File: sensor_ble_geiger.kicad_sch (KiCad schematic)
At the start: 23 parts

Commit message: power source
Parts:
- added C?: 10uF, symbol Device:C
- added C?: 33nF, symbol Device:C
- added C?: C_Polarized, symbol Device:C_Polarized
- added D?: MBRS120, symbol Device:D_Schottky
- added L?: 4.7uH, symbol Device:L
- added R?: 100k, symbol Device:R
- added R?: 47k, symbol Device:R
- added R?: 309K, symbol Device:R
- added U?: LT1308, symbol _linear-regulators:LT1308
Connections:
- net GNDD: now also C?.2, C?.2, C?.2, R?.2, U?.4 (GND)
- net VCC_5V: now also C?.1, D?.1 (K), R?.2
- new net: R?.1, R?.1, U?.2 (FB)
- new net: D?.2 (A), L?.2, U?.5 (SW)
- new net: R?.1, U?.1 (VC)
- new net: C?.1, R?.2
- new net 18660_Input: C?.1, L?.1, U?.3 (~SHDN), U?.6 (VIN)

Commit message: Добавлена разводка
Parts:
- added BZ1: Buzzer, Buzzer_Beeper:Buzzer_15x7.5RM7.6, symbol Device:Buzzer
- added C6: 470pF, Capacitor_SMD:C_0805_2012Metric, symbol Device:C
- added C8: 2.2uF, Capacitor_SMD:C_0805_2012Metric, symbol Device:C
- added D5: LED, LED_THT:LED_D3.0mm, symbol Device:LED
- added J1: Conn_01x02, Connector_PinHeader_2.54mm:PinHeader_1x02_P2.54mm_Vertical, symbol Connector_Generic:Conn_01x02
- added J2: Geiger +, Geiger:Датчик, symbol Connector_Generic:Conn_01x01
- added J3: Geiger -, Geiger:Датчик, symbol Connector_Generic:Conn_01x01
- added J4: Conn_01x04, Connector_PinHeader_2.54mm:PinHeader_1x04_P2.54mm_Horizontal, symbol Connector_Generic:Conn_01x04
- added Q4: BC847, Package_TO_SOT_SMD:SOT-23, symbol Transistor_BJT:BC847
- added R13: 510R, Resistor_SMD:R_0805_2012Metric, symbol Device:R
- added R15: 1K, Resistor_SMD:R_0805_2012Metric, symbol Device:R
- added U3: MIC5219-3.3, Package_TO_SOT_SMD:SOT-23-5, symbol Paperless_v3-rescue:MIC5219-3.3-Regulator_Linear
- added U4: E73-2G4M04S1B, Ebyte:E73-2G4M04S1B, symbol Ebyte:E73-2G4M04S1B
- C1, C11, C3, C4: renamed from C?; footprint (none) -> Resistor_SMD:R_0805_2012Metric
- C10, C7, C9: renamed from C?; footprint (none) -> Resistor_SMD:R_1210_3225Metric
- C2: renamed from C?; footprint (none) -> Resistor_THT:R_Axial_DIN0204_L3.6mm_D1.6mm_P5.08mm_Horizontal
- C5: renamed from C?; value C_Polarized -> 100uF; footprint (none) -> Resistor_THT:R_Axial_DIN0204_L3.6mm_D1.6mm_P5.08mm_Horizontal
- D1: renamed from D?; footprint (none) -> Diode_SMD:D_SMB
- L1: renamed from L?; footprint (none) -> Geiger:IND_SMD_CD43
- L2: renamed from L?; footprint (none) -> Geiger:BOURNS-SDR0503
- R1, R10, R11, R12, R2, R3, R4, R5, R6, R7, R8, R9: renamed from R?; footprint (none) -> Resistor_SMD:R_0805_2012Metric
- U2: renamed from U?; footprint (none) -> Package_SO:SO-8_5.3x6.2mm_P1.27mm
- gave numbers to parts that had none: 7
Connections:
- net 18660_Input: now also J1.2 (Pin_2), U3.1 (IN), U3.3 (EN)
- net GNDD: now also C6.2, C8.2, D5.1 (K), J1.1 (Pin_1), J4.4 (Pin_4), Q4.2 (E), U3.2 (GND), U4.1 (GND), U4.16 (GND), U4.2 (GND), U4.3 (GND), U4.43 (GND), U4.44 (GND)
- net INT_0: now reaches Q3.3 (C), R8.1
- net INT_0: now also U4.22 (P0.06)
- net at R10.2: now also J2.1 (Pin_1)
- net at C11.1, R11.1: now also J3.1 (Pin_1)
- net VCC_3.3 renamed VCC_3.3V
- net VCC_3.3V: now also BZ1.1 (-), C8.1, J4.1 (Pin_1), U3.5 (OUT), U4.17 (VCC)
- new net: J4.2 (Pin_2), U4.39 (SWDIO)
- new net: J4.3 (Pin_3), U4.38 (SWDCLK)
- new net: C6.1, U3.4 (BP)
- new net: Q4.1 (B), R15.1
- new net: BZ1.2 (+), Q4.3 (C)
- new net: D5.2 (A), R13.1
- new net BUZZER: R15.2, U4.23 (P0.07)
- new net LED: R13.2, U4.24 (P0.08)
- no-connect marks 0 -> 34

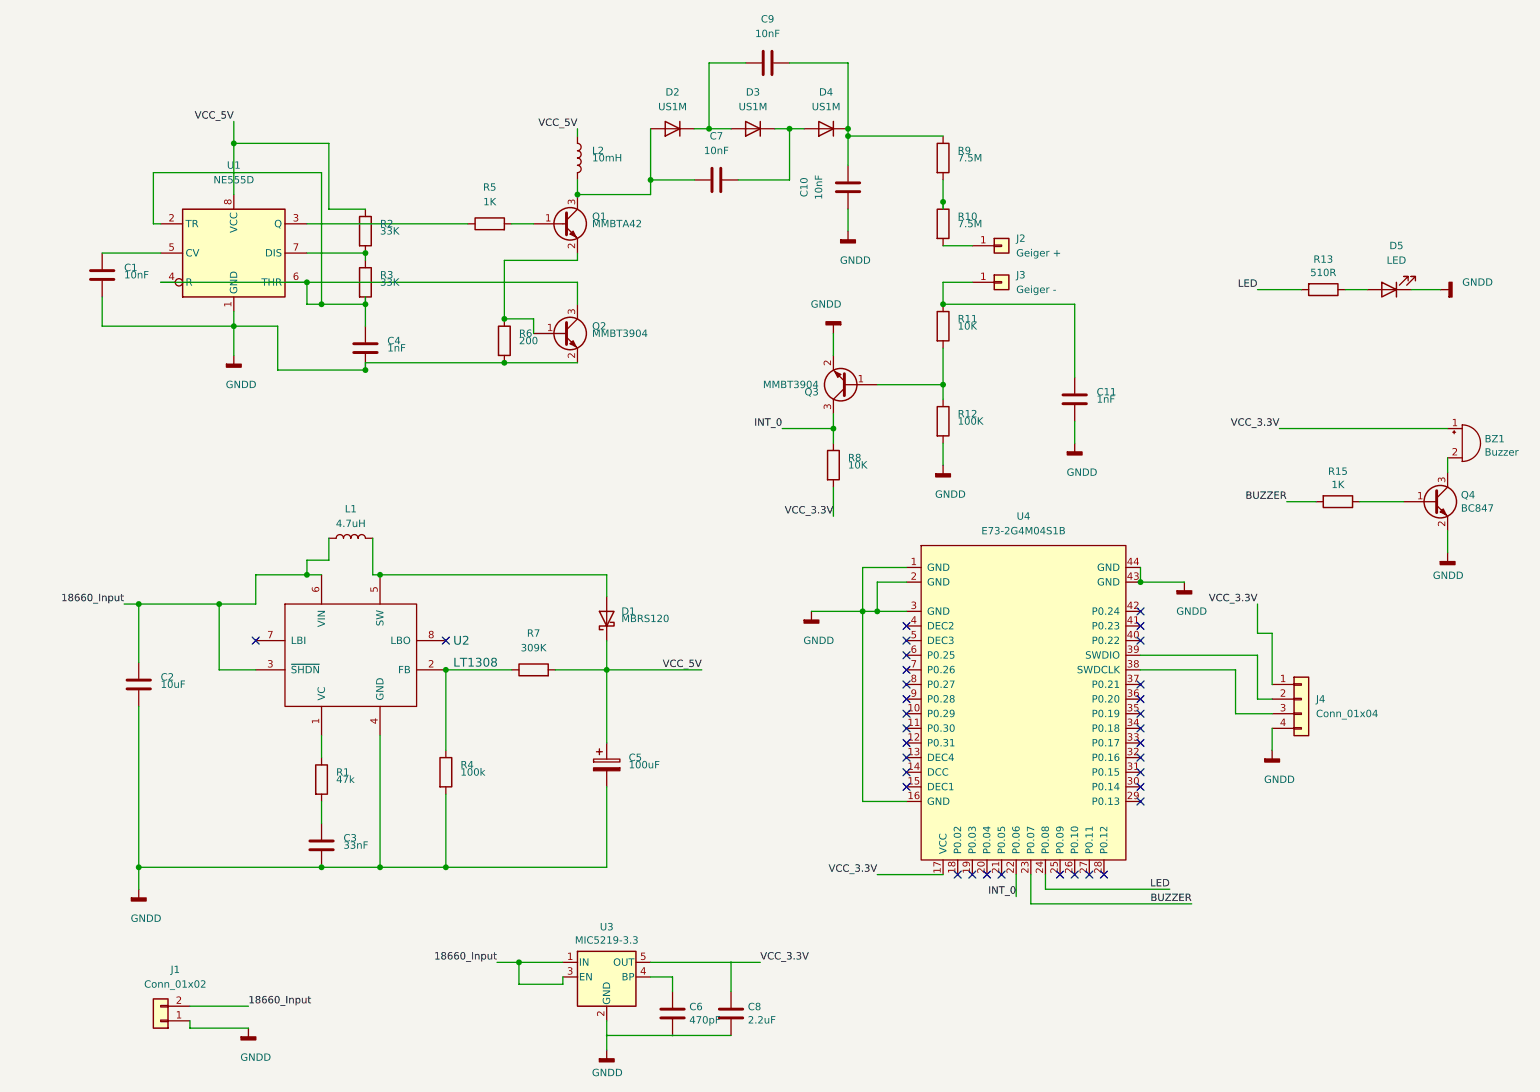
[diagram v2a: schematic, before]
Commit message: Move to 3.3V
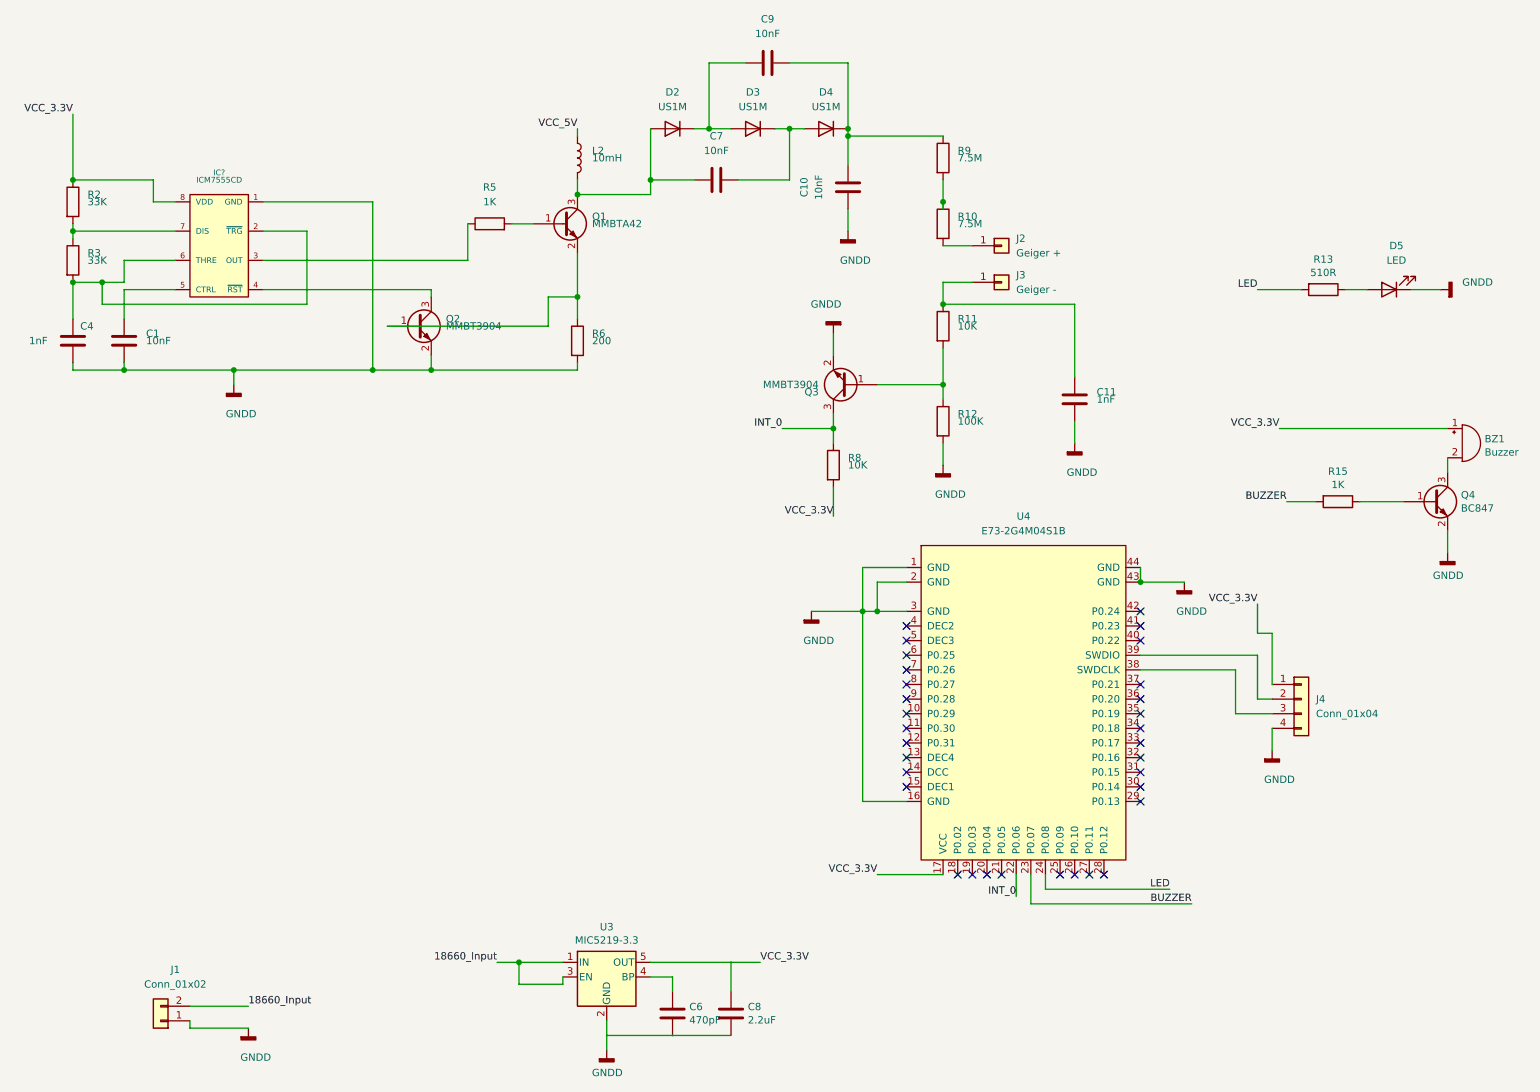
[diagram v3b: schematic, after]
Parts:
- removed C2: 10uF, Resistor_THT:R_Axial_DIN0204_L3.6mm_D1.6mm_P5.08mm_Horizontal, symbol Device:C
- removed C3: 33nF, Resistor_SMD:R_0805_2012Metric, symbol Device:C
- removed C5: 100uF, Resistor_THT:R_Axial_DIN0204_L3.6mm_D1.6mm_P5.08mm_Horizontal, symbol Device:C_Polarized
- removed D1: MBRS120, Diode_SMD:D_SMB, symbol Device:D_Schottky
- removed L1: 4.7uH, Geiger:IND_SMD_CD43, symbol Device:L
- removed R1: 47k, Resistor_SMD:R_0805_2012Metric, symbol Device:R
- removed R4: 100k, Resistor_SMD:R_0805_2012Metric, symbol Device:R
- removed R7: 309K, Resistor_SMD:R_0805_2012Metric, symbol Device:R
- removed U1: NE555D, Package_SO:SOIC-8_3.9x4.9mm_P1.27mm, symbol Timer:NE555D
- removed U2: LT1308, Package_SO:SO-8_5.3x6.2mm_P1.27mm, symbol _linear-regulators:LT1308
- added IC?: ICM7555CD, symbol ICM:ICM7555CD
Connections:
- net GNDD: now also IC?.1 (GND)
- net VCC_3.3V: now also R2.1, IC?.8 (VDD)
- net VCC_5V: no longer R2.1
- net at R2.2, R3.1: now also IC?.7 (DIS)
- net at C4.1, R3.2: now also IC?.2 (~TRG), IC?.6 (THRE); no longer Q2.3 (C)
- net at R5.1: now also IC?.3 (OUT)
- net at C1.1: now also IC?.5 (CTRL)
- new net: IC?.4 (~RST), Q2.3 (C)
- no-connect marks 34 -> 32
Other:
- moved on the sheet: C1, C4, Q2, R2, R3, R6

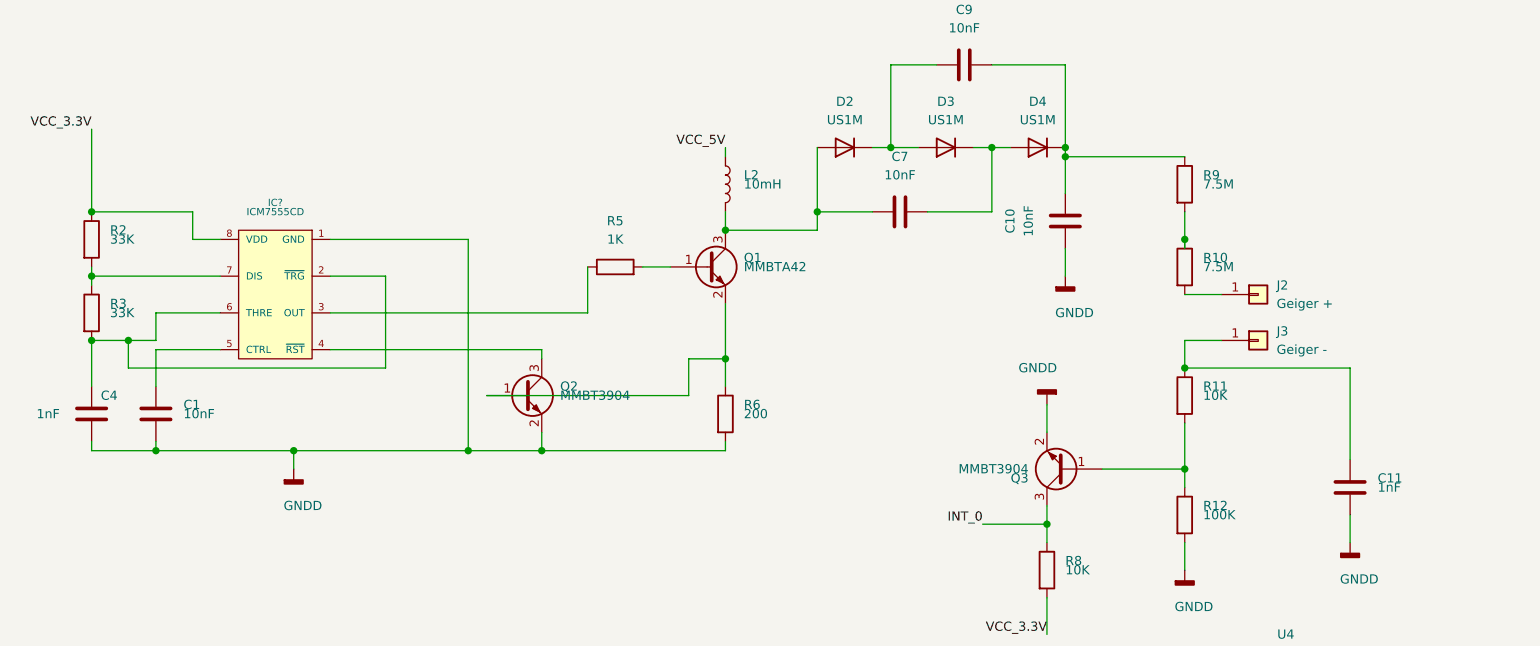
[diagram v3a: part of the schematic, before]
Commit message: Move to 3.3V
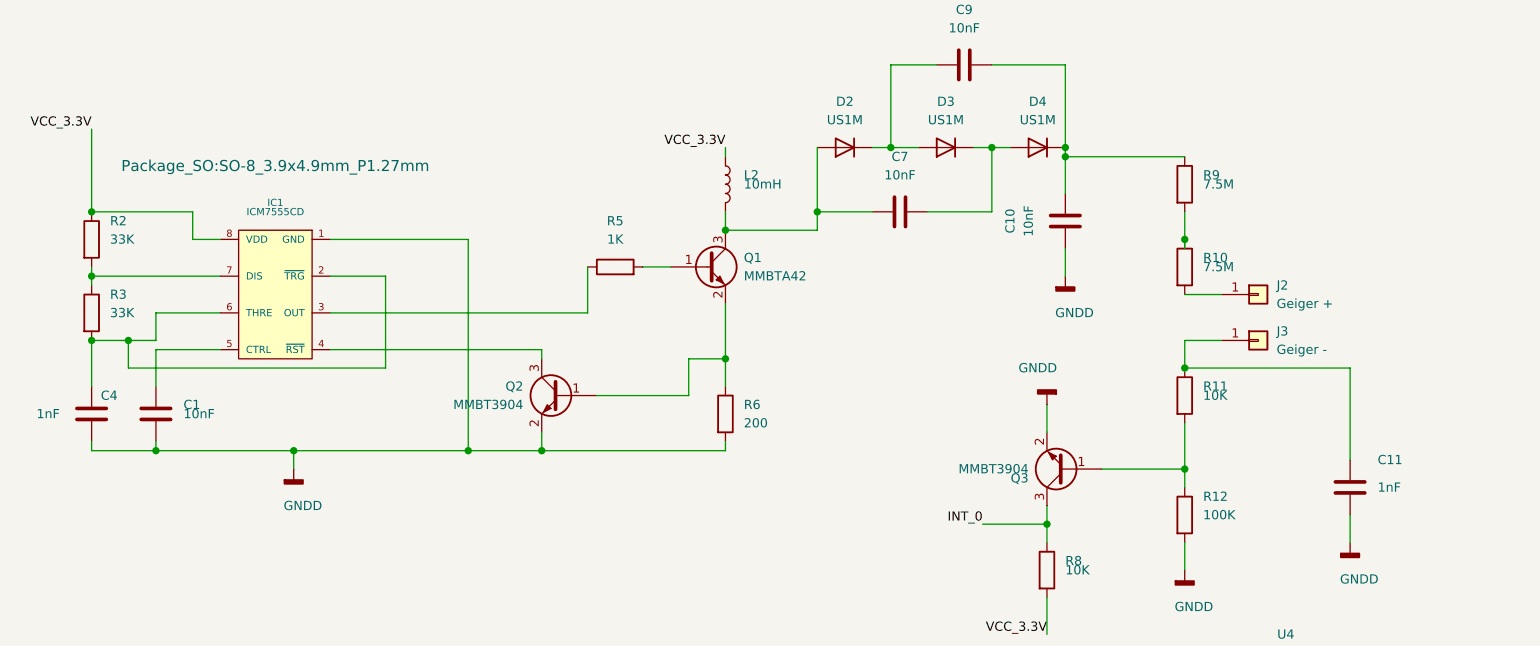
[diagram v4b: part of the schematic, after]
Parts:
- IC1: renamed from IC?; footprint (none) -> Package_SO:SO-8_3.9x4.9mm_P1.27mm
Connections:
- net VCC_5V is gone; now on net VCC_3.3V: L2.1
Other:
- moved on the sheet: Q2
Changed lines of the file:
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@@
   (junction (at 179.07 74.93) (diameter 1.016) (color 0 0 0 0))
   (junction (at 213.36 109.22) (diameter 1.016) (color 0 0 0 0))
-  (no_connect (at 199.39 160.02))
+  (no_connect (at 186.69 160.02))
+  (no_connect (at 213.36 119.38))
+  (no_connect (at 172.72 142.24))
+  (no_connect (at 213.36 114.3))
+  (no_connect (at 213.36 129.54))
+  (no_connect (at 207.01 160.02))
+  (no_connect (at 172.72 124.46))
+  (no_connect (at 213.36 144.78))
+  (no_connect (at 172.72 119.38))
+  (no_connect (at 172.72 116.84))
+  (no_connect (at 172.72 132.08))
+  (no_connect (at 213.36 116.84))
+  (no_connect (at 172.72 139.7))
+  (no_connect (at 213.36 142.24))
   (no_connect (at 213.36 137.16))
-  (no_connect (at 213.36 147.32))
-  (no_connect (at 213.36 144.78))
-  (no_connect (at 172.72 129.54))
-  (no_connect (at 172.72 144.78))
-  (no_connect (at 172.72 116.84))
-  (no_connect (at 213.36 134.62))
-  (no_connect (at 189.23 160.02))
+  (no_connect (at 172.72 121.92))
   (no_connect (at 172.72 127))
-  (no_connect (at 213.36 142.24))
-  (no_connect (at 204.47 160.02))
-  (no_connect (at 172.72 121.92))
-  (no_connect (at 213.36 116.84))
-  (no_connect (at 213.36 127))
-  (no_connect (at 186.69 160.02))
-  (no_connect (at 172.72 124.46))
-  (no_connect (at 201.93 160.02))
-  (no_connect (at 207.01 160.02))
-  (no_connect (at 213.36 129.54))
-  (no_connect (at 213.36 119.38))
   (no_connect (at 172.72 134.62))
   (no_connect (at 181.61 160.02))
+  (no_connect (at 204.47 160.02))
+  (no_connect (at 199.39 160.02))
+  (no_connect (at 172.72 137.16))
+  (no_connect (at 213.36 147.32))
+  (no_connect (at 201.93 160.02))
+  (no_connect (at 213.36 134.62))
   (no_connect (at 184.15 160.02))
+  (no_connect (at 172.72 144.78))
+  (no_connect (at 213.36 139.7))
+  (no_connect (at 213.36 127))
+  (no_connect (at 189.23 160.02))
+  (no_connect (at 172.72 129.54))
   (no_connect (at 213.36 132.08))
-  (no_connect (at 172.72 132.08))
-  (no_connect (at 213.36 114.3))
-  (no_connect (at 172.72 142.24))
-  (no_connect (at 213.36 139.7))
-  (no_connect (at 172.72 139.7))
-  (no_connect (at 172.72 119.38))
-  (no_connect (at 172.72 137.16))
   (wire (pts (xy 27.94 27.94) (xy 27.94 39.37))
     (stroke (width 0) (type solid) (color 0 0 0 0))
@@
     (stroke (width 0) (type solid) (color 0 0 0 0))
   )
-  (wire (pts (xy 82.55 64.77) (xy 110.49 64.77))
-    (stroke (width 0) (type solid) (color 0 0 0 0))
-  )
   (wire (pts (xy 90.17 58.42) (xy 60.96 58.42))
     (stroke (width 0) (type solid) (color 0 0 0 0))
@@
   )
   (wire (pts (xy 96.52 53.34) (xy 96.52 46.99))
+    (stroke (width 0) (type solid) (color 0 0 0 0))
+  )
+  (wire (pts (xy 97.79 64.77) (xy 110.49 64.77))
     (stroke (width 0) (type solid) (color 0 0 0 0))
   )
@@
     (effects (font (size 1.27 1.27)) (justify right bottom))
   )
-  (label "VCC_5V" (at 115.57 30.48 180)
+  (label "VCC_3.3V" (at 115.57 30.48 180)
     (effects (font (size 1.27 1.27)) (justify right bottom))
   )
@@
   (symbol (lib_id "Device:R") (at 27.94 43.18 0) (unit 1)
     (in_bom yes) (on_board yes)
-    (property "Reference" "R2" (id 0) (at 30.48 41.91 0)
+    (property "Reference" "R2" (id 0) (at 30.48 40.64 0)
       (effects (font (size 1.27 1.27)) (justify left))
     )
@@
   (symbol (lib_id "Device:R") (at 27.94 53.34 0) (unit 1)
     (in_bom yes) (on_board yes)
-    (property "Reference" "R3" (id 0) (at 30.48 52.07 0)
+    (property "Reference" "R3" (id 0) (at 30.48 50.8 0)
       (effects (font (size 1.27 1.27)) (justify left))
     )
@@
       (effects (font (size 1.27 1.27)) (justify left))
     )
-    (property "Value" "200" (id 1) (at 118.11 67.31 0)
+    (property "Value" "200" (id 1) (at 118.11 68.58 0)
       (effects (font (size 1.27 1.27)) (justify left))
     )
@@
   (symbol (lib_id "Device:R") (at 179.07 81.28 0) (unit 1)
     (in_bom yes) (on_board yes)
-    (property "Reference" "R12" (id 0) (at 181.61 80.01 0)
+    (property "Reference" "R12" (id 0) (at 181.61 78.74 0)
       (effects (font (size 1.27 1.27)) (justify left))
     )
@@
   (symbol (lib_id "Device:C") (at 201.93 77.47 0) (unit 1)
     (in_bom yes) (on_board yes)
-    (property "Reference" "C11" (id 0) (at 205.74 76.2 0)
+    (property "Reference" "C11" (id 0) (at 205.74 73.66 0)
       (effects (font (size 1.27 1.27)) (justify left))
     )
@@
     )
   )
-  (symbol (lib_id "Transistor_BJT:MMBT3904") (at 87.63 64.77 0) (unit 1)
-    (in_bom yes) (on_board yes)
-    (property "Reference" "Q2" (id 0) (at 92.71 63.5 0)
-      (effects (font (size 1.27 1.27)) (justify left))
-    )
-    (property "Value" "MMBT3904" (id 1) (at 92.71 64.77 0)
-      (effects (font (size 1.27 1.27)) (justify left))
-    )
-    (property "Footprint" "Package_TO_SOT_SMD:SOT-23" (id 2) (at 92.71 66.675 0)
+  (symbol (lib_id "Transistor_BJT:MMBT3904") (at 92.71 64.77 0) (mirror y) (unit 1)
+    (in_bom yes) (on_board yes)
+    (property "Reference" "Q2" (id 0) (at 87.63 63.5 0)
+      (effects (font (size 1.27 1.27)) (justify left))
+    )
+    (property "Value" "MMBT3904" (id 1) (at 87.63 66.04 0)
+      (effects (font (size 1.27 1.27)) (justify left))
+    )
+    (property "Footprint" "Package_TO_SOT_SMD:SOT-23" (id 2) (at 87.63 66.675 0)
       (effects (font (size 1.27 1.27) italic) (justify left) hide)
     )
-    (property "Datasheet" "https://www.onsemi.com/pub/Collateral/2N3903-D.PDF" (id 3) (at 87.63 64.77 0)
+    (property "Datasheet" "https://www.onsemi.com/pub/Collateral/2N3903-D.PDF" (id 3) (at 92.71 64.77 0)
       (effects (font (size 1.27 1.27)) (justify left) hide)
     )
@@
       (effects (font (size 1.27 1.27)) (justify left))
     )
-    (property "Value" "MMBTA42" (id 1) (at 118.11 46.99 0)
+    (property "Value" "MMBTA42" (id 1) (at 118.11 48.26 0)
       (effects (font (size 1.27 1.27)) (justify left))
     )
@@
   (symbol (lib_id "ICM:ICM7555CD") (at 53.34 50.8 0) (mirror y) (unit 1)
     (in_bom yes) (on_board yes)
-    (property "Reference" "IC?" (id 0) (at 53.34 38.1 0)
+    (property "Reference" "IC1" (id 0) (at 53.34 38.1 0)
       (effects (font (size 0.9906 0.9906)))
     )
@@
       (effects (font (size 0.9906 0.9906)))
     )
-    (property "Footprint" "" (id 2) (at 55.88 50.8 0)
+    (property "Footprint" "Package_SO:SO-8_3.9x4.9mm_P1.27mm" (id 2) (at 53.34 33.02 0)
       (effects (font (size 1.524 1.524)))
     )
@@
     )
     (path "/92b56e07-6413-4e00-a65f-1be269b42a72"
-      (reference "IC?") (unit 1) (value "ICM7555CD") (footprint "")
+      (reference "IC1") (unit 1) (value "ICM7555CD") (footprint "Package_SO:SO-8_3.9x4.9mm_P1.27mm")
     )
     (path "/f00e5ba8-93e3-4564-8a74-af6a75575989"
